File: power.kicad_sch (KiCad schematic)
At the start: 21 parts, among them SW101 SW_SPDT, U1 L7805

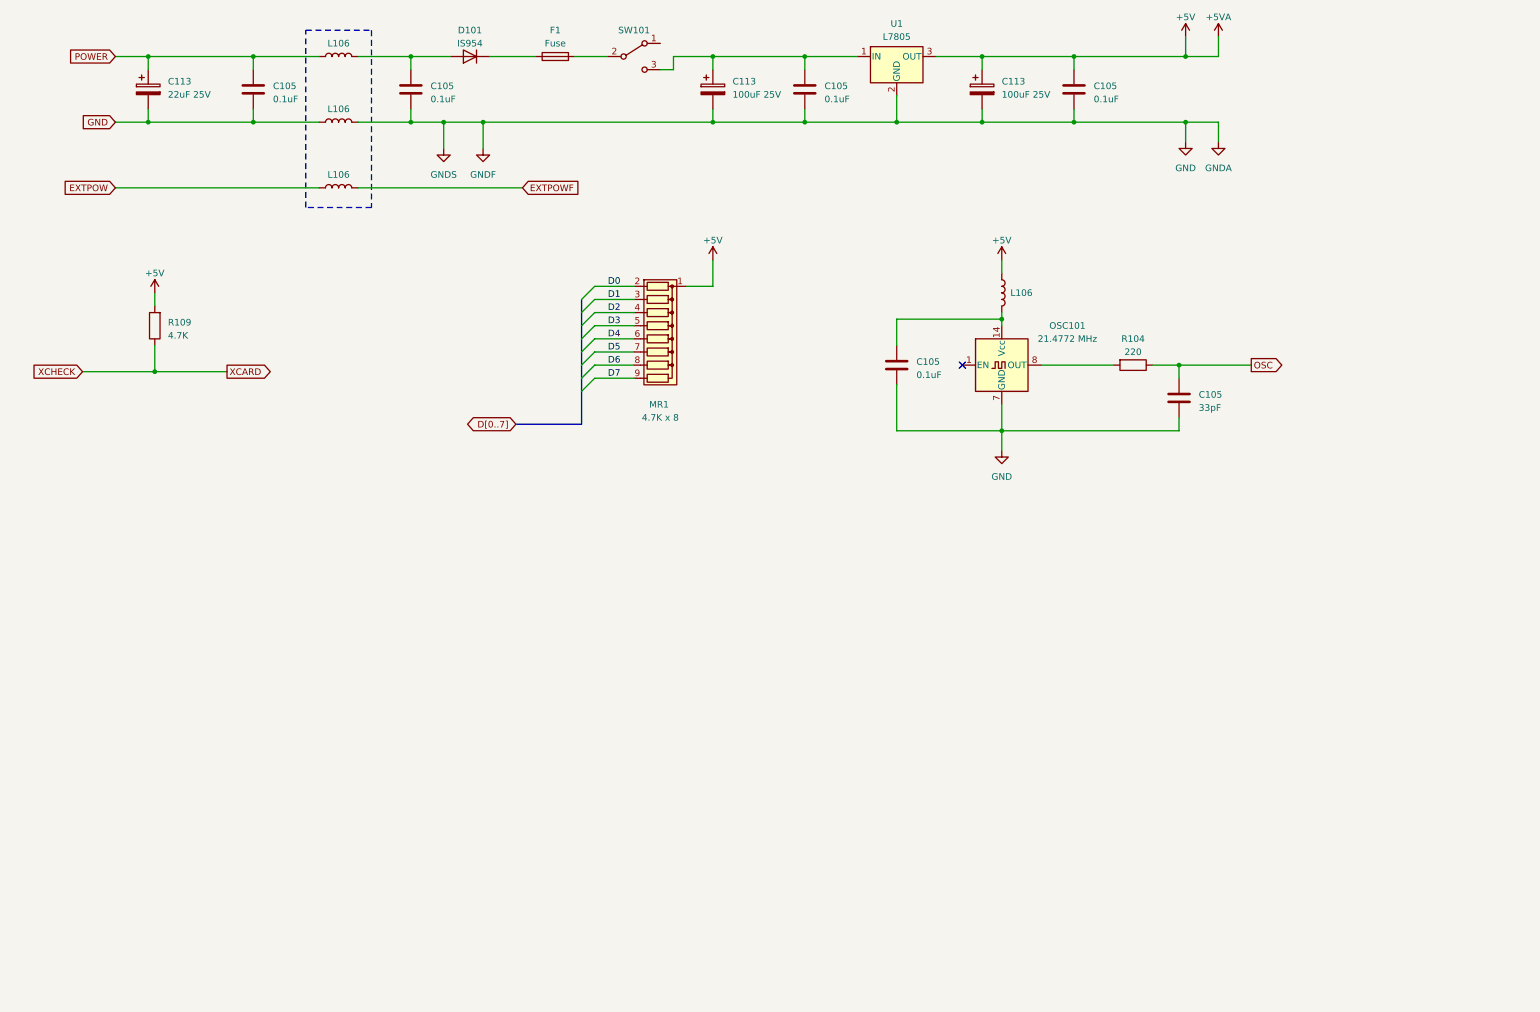
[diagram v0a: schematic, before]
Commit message: Add SMD 1206 footprint and some passives.
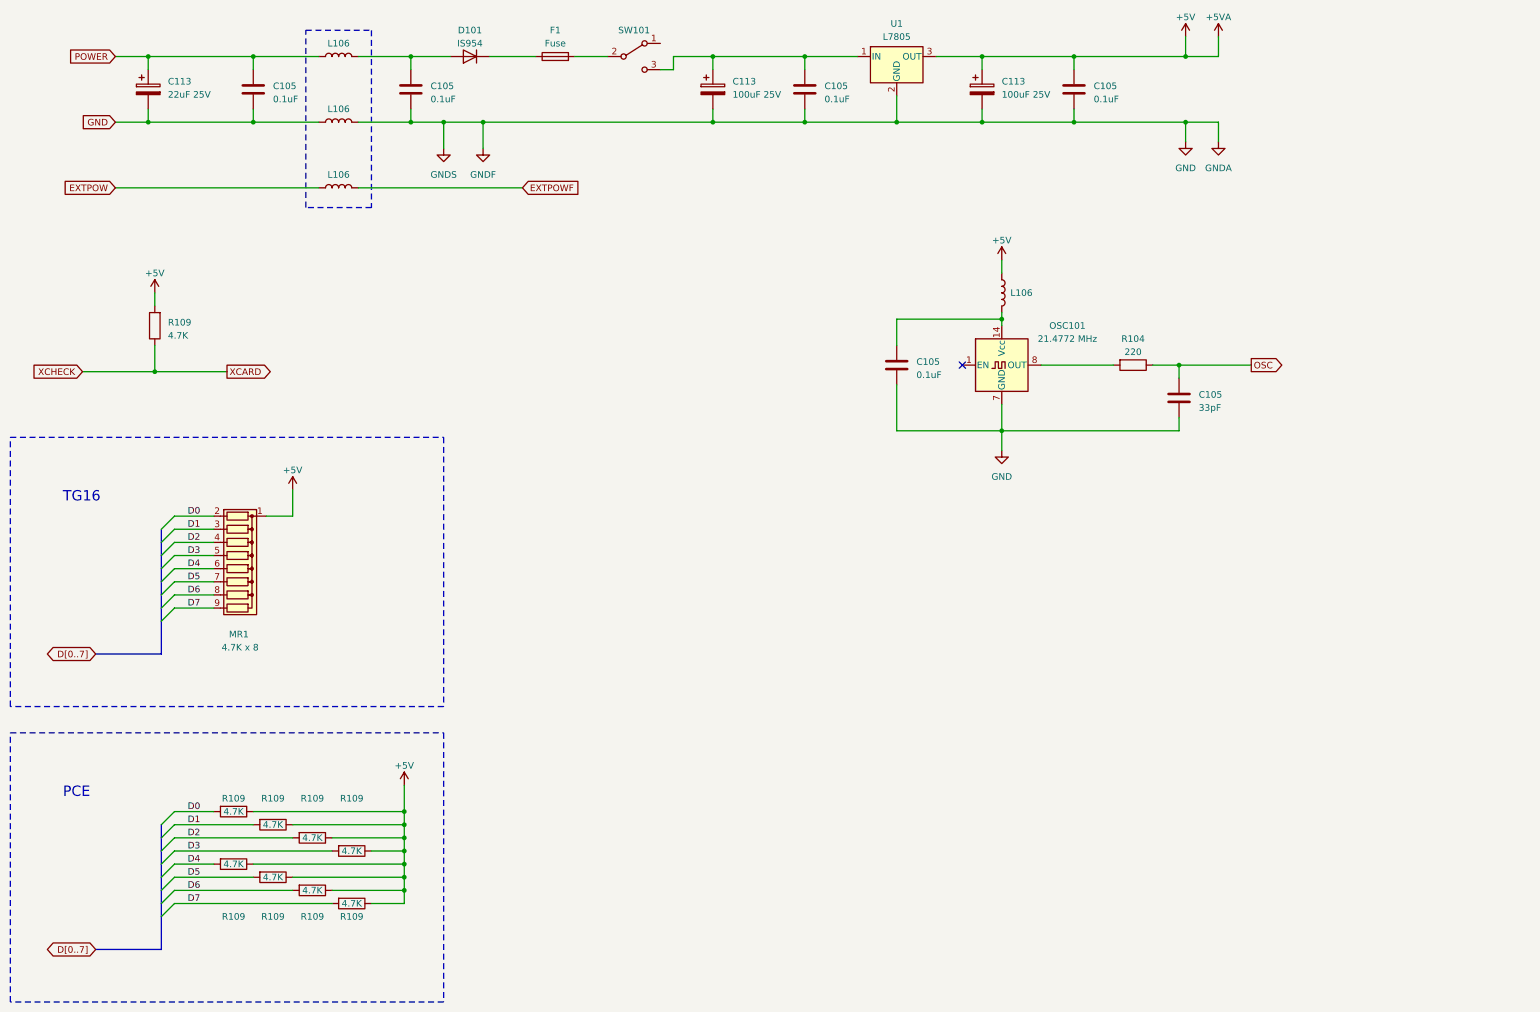
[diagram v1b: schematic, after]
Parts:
- added R109 (x8): 4.7K, A-PCENGINE:SMD_1206, symbol Device:R
- MR1: now left out of the parts list
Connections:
- net +5V: now also R109.1, R109.1, R109.1, R109.1, R109.1, R109.1, R109.1, R109.1
- net D0: now also R109.2
- net D1: now also R109.2
- net D2: now also R109.2
- net D3: now also R109.2
- net D4: now also R109.2
- net D5: now also R109.2
- net D6: now also R109.2
- net D7: now also R109.2
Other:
- note added: "PCE"
- note added: "TG16"
- moved on the sheet: MR1

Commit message: Work out numbering of and route some caps.
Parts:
- C113: footprint (none) -> A-PCENGINE:Elec_P5.00mm
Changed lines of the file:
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@@
       (effects (font (size 1.27 1.27)) (justify left))
     )
-    (property "Footprint" "" (at 160.9852 35.56 0)
+    (property "Footprint" "A-PCENGINE:Elec_P5.00mm" (at 160.9852 35.56 0)
       (effects (font (size 1.27 1.27)) hide)
     )
@@
       (effects (font (size 1.27 1.27)) (justify left))
     )
-    (property "Footprint" "" (at 51.7652 35.56 0)
+    (property "Footprint" "A-PCENGINE:Elec_P5.00mm" (at 51.7652 35.56 0)
       (effects (font (size 1.27 1.27)) hide)
     )
@@
       (effects (font (size 1.27 1.27)) (justify left))
     )
-    (property "Footprint" "" (at 213.0552 35.56 0)
-      (effects (font (size 1.27 1.27)) hide)
-    )
+    (property "Footprint" "A-PCENGINE:Elec_P5.00mm" (at 213.0552 35.56 0)
+      (effects (font (size 1.27 1.27)) hide)
+    )

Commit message: Intermediate save
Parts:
- removed C113: 22uF 25V, A-PCENGINE:Elec_P5.00mm, symbol Device:C_Polarized
- removed L106 (x2): ~, symbol Device:L
- added FL109: Filter_EMI_CommonMode, A-PCENGINE:EMI_Dual_coil, symbol Device:Filter_EMI_CommonMode
- added J2: Barrel_Jack, A-PCENGINE:Barrel_Jack, symbol Connector:Barrel_Jack
- added JP103: ~, A-PCENGINE:Jumper_Link, symbol Jumper:Jumper_2_Bridged
- added L101: Test Points, A-PCENGINE:2xTest_Point, symbol Connector_Generic:Conn_01x02
- added L106: ~, A-PCENGINE:L-5.00mm, symbol Device:L
- C105: footprint (none) -> A-PCENGINE:SMD_1206_C
- C105: value 0.1uF -> ?; footprint (none) -> A-PCENGINE:SMD_1206_C
- D101: footprint (none) -> A-PCENGINE:Diode
- FS101: renamed from F1; value Fuse -> 1A 125V; footprint (none) -> A-PCENGINE:Fuse
- IC109: renamed from U1; footprint (none) -> A-PCENGINE:IC109
- L106: footprint (none) -> A-PCENGINE:L-5.00mm
- R104, R109: footprint (none) -> A-PCENGINE:SMD_1206
- SW101: footprint (none) -> A-PCENGINE:SW101
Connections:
- net +5V: now also L106.1; no longer L106.1
- net GND: now also L106.2, FL109.3; no longer C105.2, C105.2, C105.2, OSC101.7 (GND)
- net OSC: now also C105.2
- net at C105.1, D101.2 (A): now also FL109.1
- net at C105.1, OSC101.14 (Vcc): now also L106.2; no longer L106.2
- net at OSC101.8 (OUT), R104.2: now also L101.1 (Pin_1)
- net POWER: no longer names the net of C105.1
- net POWER: now also L101.2 (Pin_2)
- new net: FL109.2, J2.2, JP103.1 (A), JP103.2 (B)
- new net: FL109.4, J2.1
- new net OSC_GND: C105.2, C105.2, L106.1, OSC101.7 (GND)
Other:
- moved on the sheet: L106

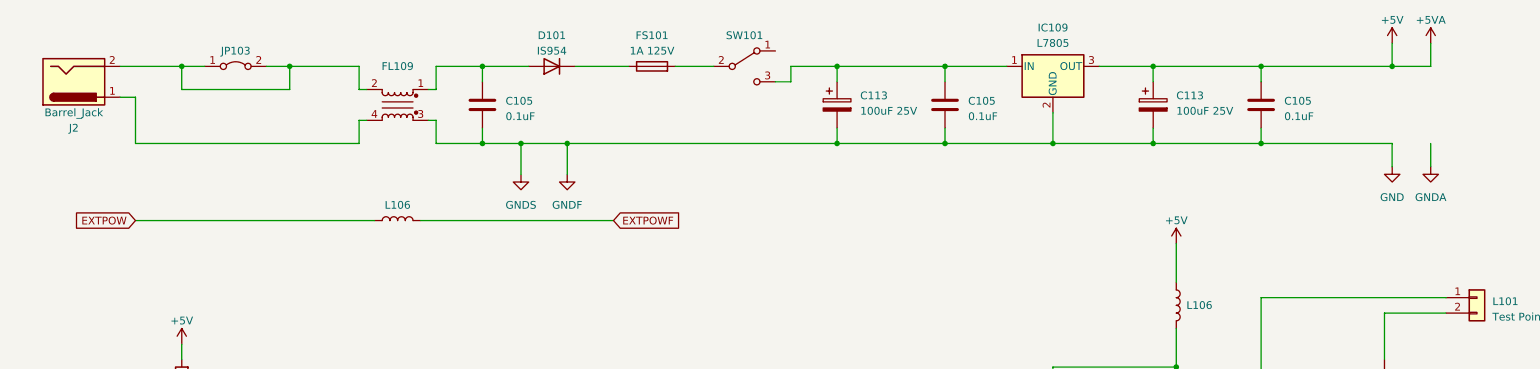
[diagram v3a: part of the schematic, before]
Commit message: Finish basic routing, resolve DRC errors.
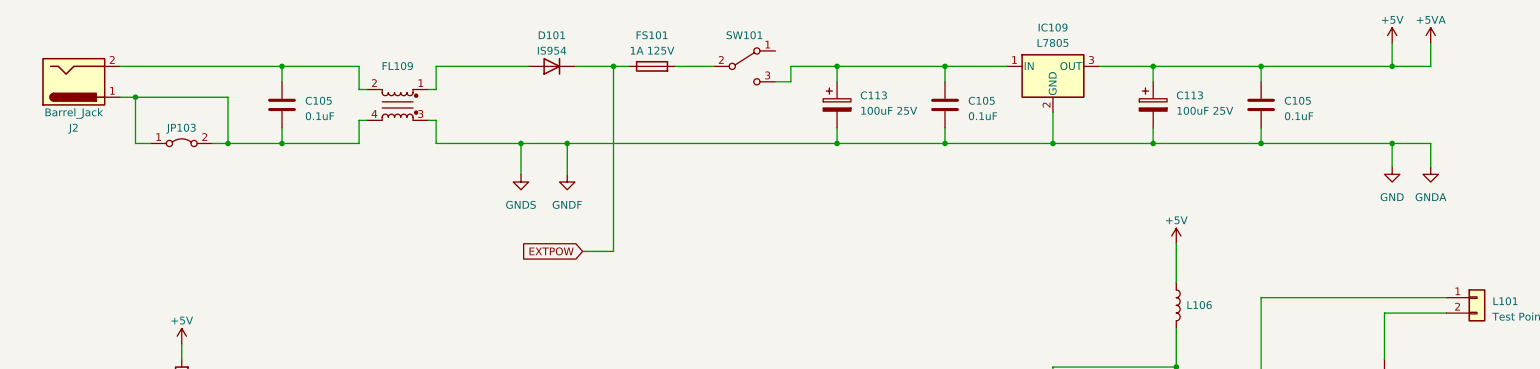
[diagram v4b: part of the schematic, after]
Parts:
- removed L106: ~, symbol Device:L
- C105: footprint A-PCENGINE:SMD_1206_C -> A-PCENGINE:SMD_1206
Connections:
- net EXTPOW: now also D101.1 (K), FS101.1
- net GND: no longer C105.2
- net at D101.2 (A), FL109.1: no longer C105.1
- net at FL109.2, J2.2: now also C105.1; no longer JP103.1 (A), JP103.2 (B)
- net at FL109.4, J2.1: now also C105.2, JP103.1 (A), JP103.2 (B)
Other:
- moved on the sheet: JP103

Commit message: First draft of complete PCB.
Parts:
- removed MR1: 4.7K x 8, Resistor_THT:R_Array_SIP9, symbol Device:R_Network08
- R104: value 220 -> 100
- SW101: symbol Switch:SW_SPDT -> PC-Engine:SW_SPDT
- renumbered J2 to CN104
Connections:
- net OSC_GND is gone; now on net GND: C105.2, C105.2, L106.1, OSC101.7 (GND)
- net GND: now also SW101.0 (CASE)
- net at C105.1, C113.1, IC109.1 (IN): now also SW101.1 (A); no longer SW101.3 (C)
- no-connect marks 1 -> 2
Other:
- note added: "Ground routed separately for oscillator"
- note removed: "PCE"
- note removed: "TG16"
- moved on the sheet: C105, D101, FS101, L101, L106, OSC101, R104, R109

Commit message: Verify passive values.
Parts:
- C105: value ? -> N/P
- C113: value 100uF 25V -> 47uF 25V
- C113: value 100uF 25V -> 47uF 16V
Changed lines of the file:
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@@
       (effects (font (size 1.27 1.27)) (justify left))
     )
-    (property "Value" "100uF 25V" (at 163.83 32.766 0)
+    (property "Value" "47uF 25V" (at 163.83 32.766 0)
       (effects (font (size 1.27 1.27)) (justify left))
     )
@@
       (effects (font (size 1.27 1.27)) (justify left))
     )
-    (property "Value" "?" (at 222.25 98.425 0)
+    (property "Value" "N/P" (at 222.25 98.425 0)
       (effects (font (size 1.27 1.27)) (justify left))
     )
@@
       (effects (font (size 1.27 1.27)) (justify left))
     )
-    (property "Value" "100uF 25V" (at 215.9 32.766 0)
-      (effects (font (size 1.27 1.27)) (justify left))
-    )
+    (property "Value" "47uF 16V" (at 215.9 32.766 0)
+      (effects (font (size 1.27 1.27)) (justify left))
+    )

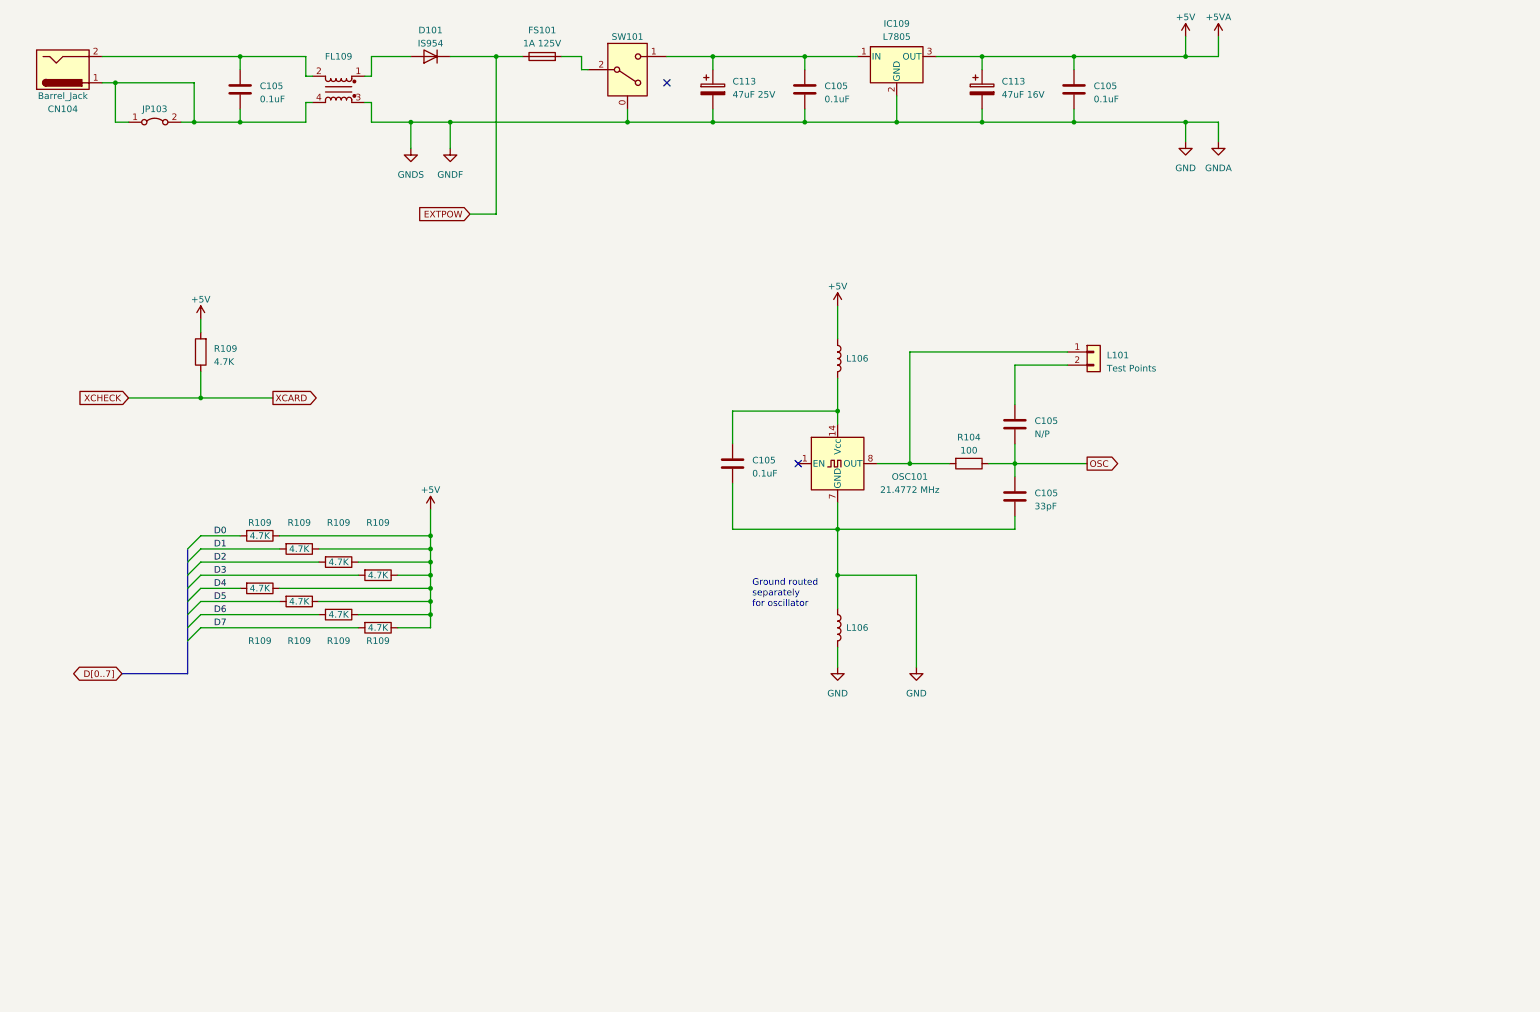
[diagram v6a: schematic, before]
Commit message: Silkscreen stuff, tidy schematics, corrections.
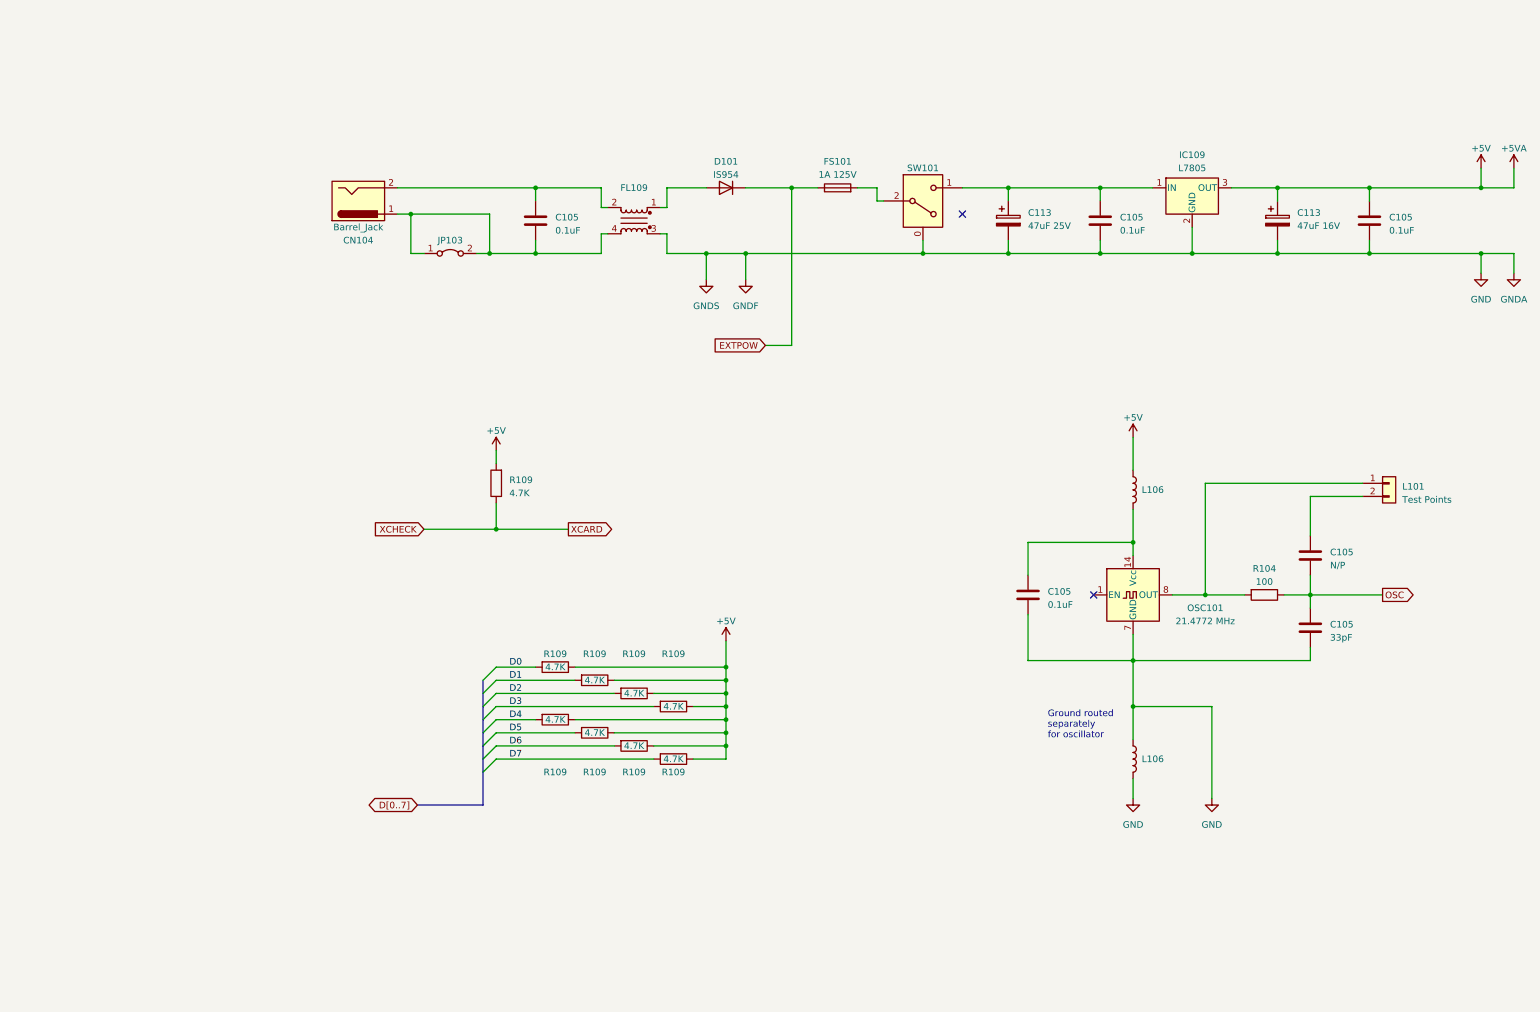
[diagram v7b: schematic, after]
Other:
- title: (none) -> PC Engine Power, Oscillator and Misc.
- moved on the sheet: C105, C113, CN104, D101, FL109, FS101, IC109, JP103, L101, L106, OSC101, R104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

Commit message: Silkscreen/DRC fixes
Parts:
- L106: footprint A-PCENGINE:L-5.00mm -> A-PCENGINE:L-5.00mm_Small_Silk
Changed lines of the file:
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@@
       (effects (font (size 1.27 1.27)))
     )
-    (property "Footprint" "A-PCENGINE:L-5.00mm" (at 241.3 161.29 0)
+    (property "Footprint" "A-PCENGINE:L-5.00mm_Small_Silk" (at 241.3 161.29 0)
       (effects (font (size 1.27 1.27)) hide)
     )
